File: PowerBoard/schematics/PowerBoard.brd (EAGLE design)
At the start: 139.7 x 44.1 mm, 59 parts, among them IC100 LM317MABDT, IC200 LM317MABDT, IC300 337, X1 22-27-2031-03, X2 22-27-2031-03, X3 22-27-2031-03, X4 22-27-2031-03

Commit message: changed component values
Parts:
- C100, C105, C200, C205, C300, C305: value (none) -> dnp
- C101, C104, C201, C204, C302, C304: value 100u -> 10u
- R1, R2, R3: value 1K -> 1k
- R201: value 220R -> 330R
- R202: value 730R -> 1k
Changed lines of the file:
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@@
 <attribute name="NAME" x="21.59" y="17.018" size="1.016" layer="25" font="vector" rot="R180" align="bottom-center"/>
 </element>
-<element name="R201" library="Rebel" package="0603" value="220R" x="54.61" y="17.78" smashed="yes" rot="R180">
+<element name="R201" library="Rebel" package="0603" value="330R" x="54.61" y="17.78" smashed="yes" rot="R180">
 <attribute name="NAME" x="54.61" y="17.018" size="1.016" layer="25" font="vector" rot="R180" align="bottom-center"/>
 </element>
@@
 <attribute name="NAME" x="21.59" y="11.557" size="1.016" layer="25" font="vector" align="bottom-center"/>
 </element>
-<element name="R202" library="Rebel" package="0603" value="730R" x="54.61" y="13.97" smashed="yes">
+<element name="R202" library="Rebel" package="0603" value="1k" x="54.61" y="13.97" smashed="yes">
 <attribute name="NAME" x="54.61" y="13.208" size="1.016" layer="25" font="vector" rot="R180" align="bottom-center"/>
 </element>
@@
 <attribute name="NAME" x="87.63" y="13.208" size="1.016" layer="25" font="vector" rot="R180" align="bottom-center"/>
 </element>
-<element name="C302" library="rcl" package="153CLV-0810" value="100u" x="87.63" y="26.67" smashed="yes" rot="R90">
+<element name="C302" library="rcl" package="153CLV-0810" value="10u" x="87.63" y="26.67" smashed="yes" rot="R90">
 <attribute name="NAME" x="93.26" y="24.285" size="1.27" layer="25" rot="R90"/>
 <attribute name="VALUE" x="93.415" y="22.345" size="1.27" layer="27" rot="R90"/>
 </element>
-<element name="C104" library="rcl" package="153CLV-0810" value="100u" x="21.59" y="26.67" smashed="yes" rot="R270">
+<element name="C104" library="rcl" package="153CLV-0810" value="10u" x="21.59" y="26.67" smashed="yes" rot="R270">
 <attribute name="NAME" x="27.22" y="24.285" size="1.27" layer="25" rot="R90"/>
 <attribute name="VALUE" x="15.805" y="30.995" size="1.27" layer="27" rot="R270"/>
 </element>
-<element name="C204" library="rcl" package="153CLV-0810" value="100u" x="54.61" y="26.67" smashed="yes" rot="R270">
+<element name="C204" library="rcl" package="153CLV-0810" value="10u" x="54.61" y="26.67" smashed="yes" rot="R270">
 <attribute name="NAME" x="60.24" y="24.285" size="1.27" layer="25" rot="R90"/>
 <attribute name="VALUE" x="48.825" y="30.995" size="1.27" layer="27" rot="R270"/>
 </element>
-<element name="C304" library="rcl" package="153CLV-0810" value="100u" x="100.33" y="26.67" smashed="yes" rot="R90">
+<element name="C304" library="rcl" package="153CLV-0810" value="10u" x="100.33" y="26.67" smashed="yes" rot="R90">
 <attribute name="NAME" x="105.96" y="24.285" size="1.27" layer="25" rot="R90"/>
 <attribute name="VALUE" x="106.115" y="22.345" size="1.27" layer="27" rot="R90"/>
@@
 <attribute name="VALUE" x="120.65" y="15.24" size="1.27" layer="27"/>
 </element>
-<element name="R1" library="Rebel" package="0603" value="1K" x="127" y="27.94" rot="R180"/>
-<element name="R2" library="Rebel" package="0603" value="1K" x="127" y="30.48" rot="R180"/>
-<element name="R3" library="Rebel" package="0603" value="1K" x="127" y="17.78" rot="R180"/>
+<element name="R1" library="Rebel" package="0603" value="1k" x="127" y="27.94" rot="R180"/>
+<element name="R2" library="Rebel" package="0603" value="1k" x="127" y="30.48" rot="R180"/>
+<element name="R3" library="Rebel" package="0603" value="1k" x="127" y="17.78" rot="R180"/>
 <element name="C103" library="rcl" package="C0603" value="1u" x="35.56" y="17.78" smashed="yes">
 <attribute name="NAME" x="33.655" y="15.875" size="1.016" layer="25"/>
@@
 <attribute name="VALUE" x="69.596" y="8.509" size="0.4064" layer="27" rot="R180"/>
 </element>
-<element name="C101" library="rcl" package="153CLV-0810" value="100u" x="34.29" y="26.67" smashed="yes" rot="R270">
+<element name="C101" library="rcl" package="153CLV-0810" value="10u" x="34.29" y="26.67" smashed="yes" rot="R270">
 <attribute name="NAME" x="39.92" y="24.285" size="1.27" layer="25" rot="R90"/>
 <attribute name="VALUE" x="28.505" y="30.995" size="1.27" layer="27" rot="R270"/>
 </element>
-<element name="C201" library="rcl" package="153CLV-0810" value="100u" x="67.31" y="26.67" smashed="yes" rot="R270">
+<element name="C201" library="rcl" package="153CLV-0810" value="10u" x="67.31" y="26.67" smashed="yes" rot="R270">
 <attribute name="NAME" x="72.94" y="24.285" size="1.27" layer="25" rot="R90"/>
 <attribute name="VALUE" x="61.525" y="30.995" size="1.27" layer="27" rot="R270"/>
@@
 <attribute name="VALUE" x="102.235" y="15.875" size="1.27" layer="27" rot="R180"/>
 </element>
-<element name="C100" library="rcl" package="E5-8,5" value="" x="34.29" y="35.56" smashed="yes" rot="R180">
+<element name="C100" library="rcl" package="E5-8,5" value="dnp" x="34.29" y="35.56" smashed="yes" rot="R180">
 <attribute name="NAME" x="39.116" y="35.8648" size="1.27" layer="25" ratio="10" rot="R270"/>
 <attribute name="VALUE" x="36.8046" y="38.5826" size="1.27" layer="27" ratio="10" rot="R180"/>
 </element>
-<element name="C200" library="rcl" package="E5-8,5" value="" x="67.31" y="35.56" smashed="yes" rot="R180">
+<element name="C200" library="rcl" package="E5-8,5" value="dnp" x="67.31" y="35.56" smashed="yes" rot="R180">
 <attribute name="NAME" x="72.136" y="35.8648" size="1.27" layer="25" ratio="10" rot="R270"/>
 <attribute name="VALUE" x="69.8246" y="38.5826" size="1.27" layer="27" ratio="10" rot="R180"/>
 </element>
-<element name="C300" library="rcl" package="E5-8,5" value="" x="87.63" y="35.56" smashed="yes" rot="R180">
+<element name="C300" library="rcl" package="E5-8,5" value="dnp" x="87.63" y="35.56" smashed="yes" rot="R180">
 <attribute name="NAME" x="92.456" y="35.8648" size="1.27" layer="25" ratio="10" rot="R270"/>
 <attribute name="VALUE" x="90.1446" y="38.5826" size="1.27" layer="27" ratio="10" rot="R180"/>
 </element>
-<element name="C105" library="rcl" package="E5-8,5" value="" x="21.59" y="35.56" smashed="yes" rot="R180">
+<element name="C105" library="rcl" package="E5-8,5" value="dnp" x="21.59" y="35.56" smashed="yes" rot="R180">
 <attribute name="NAME" x="26.416" y="35.8648" size="1.27" layer="25" ratio="10" rot="R270"/>
 <attribute name="VALUE" x="24.1046" y="38.5826" size="1.27" layer="27" ratio="10" rot="R180"/>
 </element>
-<element name="C205" library="rcl" package="E5-8,5" value="" x="54.61" y="35.56" smashed="yes" rot="R180">
+<element name="C205" library="rcl" package="E5-8,5" value="dnp" x="54.61" y="35.56" smashed="yes" rot="R180">
 <attribute name="NAME" x="59.436" y="35.8648" size="1.27" layer="25" ratio="10" rot="R270"/>
 <attribute name="VALUE" x="57.1246" y="38.5826" size="1.27" layer="27" ratio="10" rot="R180"/>
 </element>
-<element name="C305" library="rcl" package="E5-8,5" value="" x="100.33" y="35.56" smashed="yes" rot="R180">
+<element name="C305" library="rcl" package="E5-8,5" value="dnp" x="100.33" y="35.56" smashed="yes" rot="R180">
 <attribute name="NAME" x="105.156" y="35.8648" size="1.27" layer="25" ratio="10" rot="R270"/>
 <attribute name="VALUE" x="102.8446" y="38.5826" size="1.27" layer="27" ratio="10" rot="R180"/>

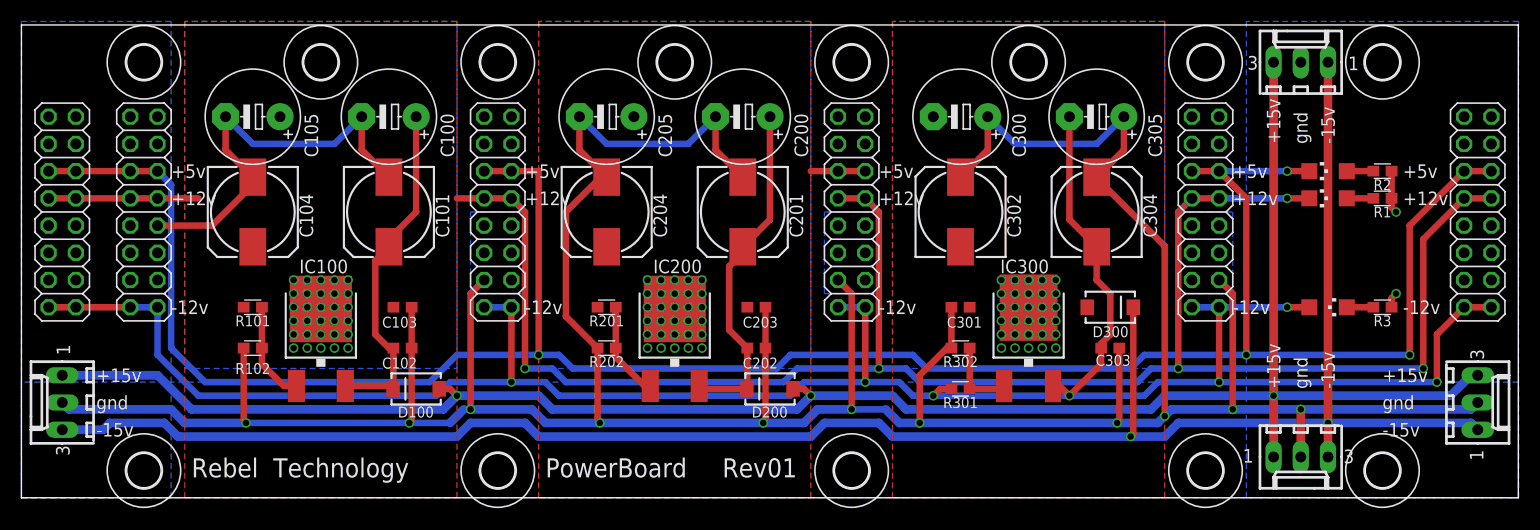
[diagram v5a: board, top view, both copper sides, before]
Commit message: added cv/gate routing, extra power header, 1206 cap footprints
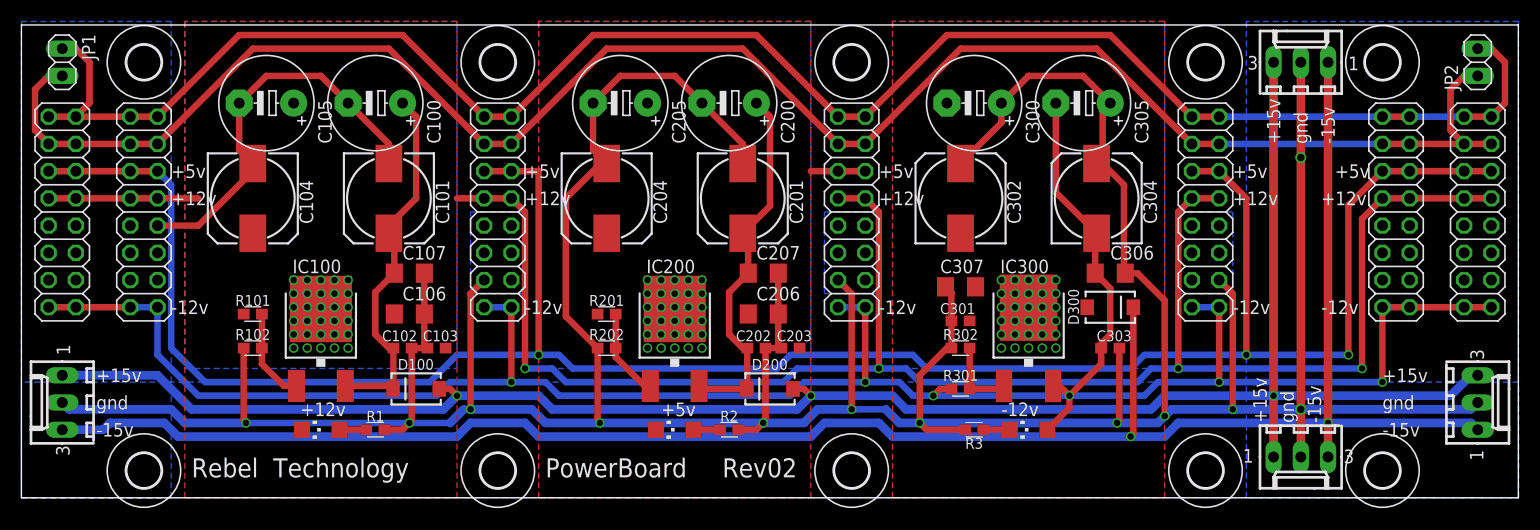
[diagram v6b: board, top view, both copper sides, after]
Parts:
- removed U$10, U$11, U$9: (no value), holes:3,2
- added C106, C107, C206, C207, C306, C307: (no value), rcl:C1206
- added JP1, JP2: (no value), pinhead:1X02
- added OUT6: M08X2, SparkFun:2X8
- moved LED1 96.4 mm to (27.9, 6.35)
- moved R1 96.4 mm to (33.0, 6.35)
- moved LED2 65.6 mm to (61.0, 6.35)
- moved R2 65.6 mm to (66.0, 6.35)
- moved R3 39.8 mm to (88.9, 6.35), turned to 0 degrees
- moved LED3 30.2 mm to (94.0, 6.35), turned to 90 degrees
- moved C103 4.96 mm to (38.7, 14.0), turned to 180 degrees
- moved C203 4.96 mm to (71.8, 14.0), turned to 180 degrees
- moved C300 1.80 mm to (88.9, 36.8)
- moved C205 1.80 mm to (55.9, 36.8)
- moved C105 1.80 mm to (22.9, 36.8)
- moved C100 1.80 mm to (33.0, 36.8)
- moved C200 1.80 mm to (66.0, 36.8)
- moved C305 1.80 mm to (99.1, 36.8)
- moved C101 1.27 mm to (34.3, 27.9)
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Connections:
- new net N$10: JP1.2, JP2.1, OUT.13, OUT.14, OUT1.13, OUT1.14, OUT2.13, OUT2.14, OUT3.13, OUT3.14, OUT4.13, OUT4.14, OUT5.13, OUT5.14, OUT6.13, OUT6.14
- new net N$12: JP1.1, JP2.2, OUT.15, OUT.16, OUT1.15, OUT1.16, OUT2.15, OUT2.16, OUT3.15, OUT3.16, OUT4.15, OUT4.16, OUT5.15, OUT5.16, OUT6.15, OUT6.16
- net +12V: now also C106.1, OUT6.10, OUT6.9
- net +5V: now also C206.1, OUT6.11, OUT6.12
- net -12V: now also C306.1, OUT6.1, OUT6.2
- net GND: now also C106.2, C107.2, C206.2, C207.2, C306.2, C307.1, OUT6.3, OUT6.4, OUT6.5, OUT6.6, OUT6.7, OUT6.8
- net N$6: now also C307.2
- net N$7: now also C207.1
- net N$8: now also C107.1
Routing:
- net N$10: track 0.00 -> 174.1 mm
- net N$12: track 0.00 -> 170.9 mm
- net GND: track 378.3 -> 422.9 mm, vias 13 -> 12
- net +5V: track 225.5 -> 218.2 mm, vias 34 -> 33
- net +12V: track 187.7 -> 180.4 mm, vias 35 -> 34
- net N$7: track 32.3 -> 34.7 mm
- net N$8: track 32.5 -> 34.7 mm
- net -12V: track 218.8 -> 217.8 mm, vias 7 -> 6
- net N$4: track 9.23 -> 8.60 mm
- net N$3: track 9.36 -> 8.73 mm
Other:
- board text added: "Rev02"
- board text removed: "Rev01"

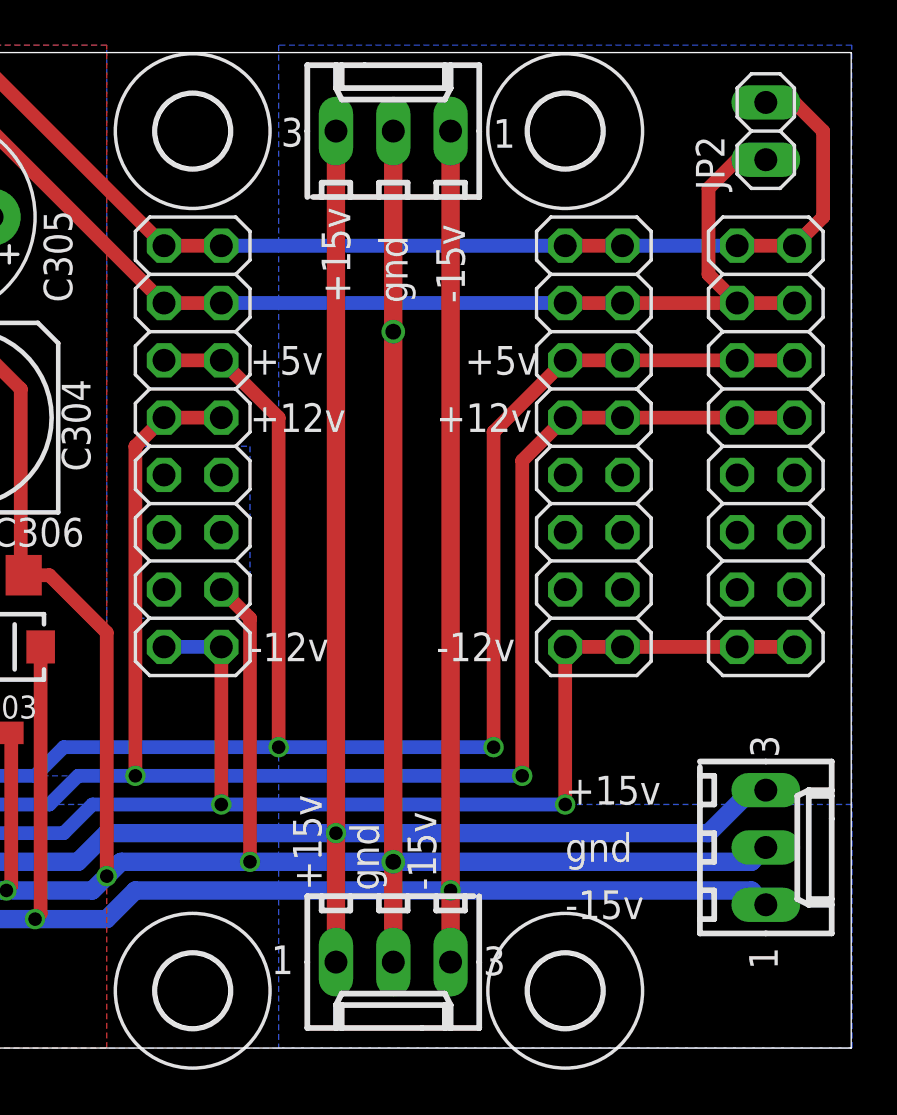
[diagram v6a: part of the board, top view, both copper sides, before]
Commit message: added measurement and adjusted ground plane
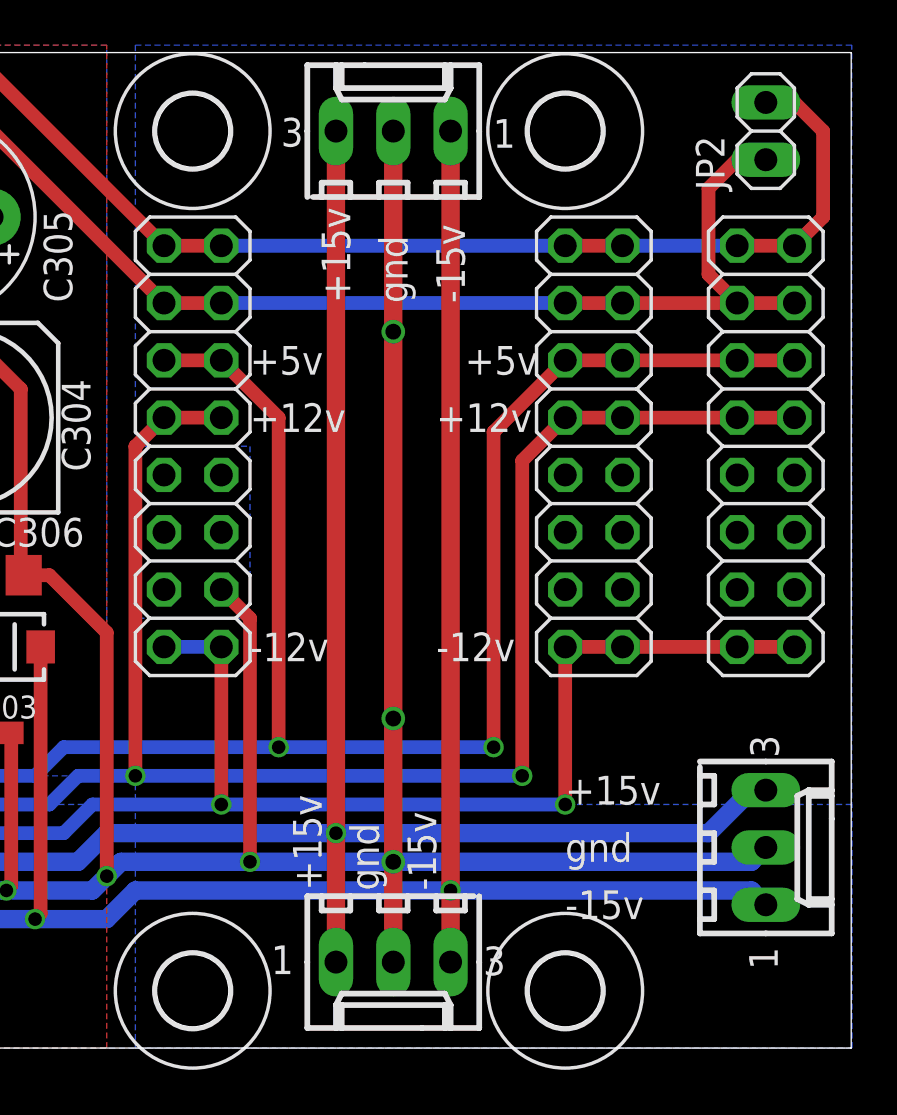
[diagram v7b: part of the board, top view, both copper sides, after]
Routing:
- net GND: vias 12 -> 13
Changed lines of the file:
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@@
 <layer number="29" name="tStop" color="7" fill="3" visible="no" active="yes"/>
 <layer number="30" name="bStop" color="7" fill="6" visible="no" active="yes"/>
-<layer number="31" name="tCream" color="7" fill="4" visible="no" active="yes"/>
-<layer number="32" name="bCream" color="7" fill="5" visible="no" active="yes"/>
+<layer number="31" name="tCream" color="7" fill="4" visible="yes" active="yes"/>
+<layer number="32" name="bCream" color="7" fill="5" visible="yes" active="yes"/>
 <layer number="33" name="tFinish" color="6" fill="3" visible="no" active="yes"/>
 <layer number="34" name="bFinish" color="6" fill="6" visible="no" active="yes"/>
@@
 <layer number="37" name="tTest" color="7" fill="1" visible="no" active="yes"/>
 <layer number="38" name="bTest" color="7" fill="1" visible="no" active="yes"/>
-<layer number="39" name="tKeepout" color="4" fill="11" visible="yes" active="yes"/>
-<layer number="40" name="bKeepout" color="1" fill="11" visible="yes" active="yes"/>
-<layer number="41" name="tRestrict" color="4" fill="10" visible="yes" active="yes"/>
-<layer number="42" name="bRestrict" color="1" fill="10" visible="yes" active="yes"/>
-<layer number="43" name="vRestrict" color="2" fill="10" visible="yes" active="yes"/>
+<layer number="39" name="tKeepout" color="4" fill="11" visible="no" active="yes"/>
+<layer number="40" name="bKeepout" color="1" fill="11" visible="no" active="yes"/>
+<layer number="41" name="tRestrict" color="4" fill="10" visible="no" active="yes"/>
+<layer number="42" name="bRestrict" color="1" fill="10" visible="no" active="yes"/>
+<layer number="43" name="vRestrict" color="2" fill="10" visible="no" active="yes"/>
 <layer number="44" name="Drills" color="7" fill="1" visible="no" active="yes"/>
 <layer number="45" name="Holes" color="7" fill="1" visible="no" active="yes"/>
-<layer number="46" name="Milling" color="3" fill="1" visible="no" active="yes"/>
+<layer number="46" name="Milling" color="3" fill="1" visible="yes" active="yes"/>
 <layer number="47" name="Measures" color="7" fill="1" visible="yes" active="yes"/>
 <layer number="48" name="Document" color="7" fill="1" visible="yes" active="yes"/>
@@
 <text x="59.69" y="7.62" size="1.27" layer="21" font="vector">+5v</text>
 <text x="91.44" y="7.62" size="1.27" layer="21" font="vector">-12v</text>
+<dimension x1="0" y1="0" x2="0" y2="44.12" x3="-2.54" y3="22.06" textsize="1.778" layer="47"/>
 </plain>
 <attributes>
@@
 </polygon>
 <polygon width="0.6096" layer="16">
-<vertex x="114.3" y="44.45"/>
-<vertex x="114.3" y="0"/>
+<vertex x="107.95" y="44.45"/>
+<vertex x="107.95" y="0"/>
 <vertex x="139.7" y="0"/>
 <vertex x="139.7" y="44.45"/>
@@
 <wire x1="119.38" y1="3.81" x2="119.38" y2="31.75" width="0.8128" layer="1"/>
 <wire x1="119.38" y1="40.64" x2="119.38" y2="31.75" width="0.8128" layer="1"/>
+<via x="119.38" y="14.605" extent="1-16" drill="0.7"/>
 </signal>
 <signal name="N$1">
